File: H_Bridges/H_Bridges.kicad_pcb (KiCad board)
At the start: 2 copper layers, 59 parts, among them J1 S4B-PH-K-SLFSN, J2 USB4085-GF-A_REVB, Q1 IRF540NSTRLPBF, Q10 PMOS, Q2 IRF540NSTRLPBF, Q3 IRF540NSTRLPBF, Q4 IRF540NSTRLPBF, Q5 IRF540NSTRLPBF, Q6 IRF540NSTRLPBF, Q7 IRF540NSTRLPBF, Q8 IRF540NSTRLPBF, Q9 PMOS, U1 ESP8266, U2 max1898eub42+T, U3 TPS61023DRLR

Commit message: started placement
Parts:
- moved U1 129.9 mm to (237.8, 145.4), turned to -90 degrees
- moved R5 107.2 mm to (241.7, 74.0)
- moved R6 102.7 mm to (241.7, 67.1)
- moved R7 102.7 mm to (241.7, 69.6)
- moved R8 102.7 mm to (241.7, 72.1)
- moved FB1 97.2 mm to (64.9, 99.6)
- moved R13 89.8 mm to (55.6, 96.3), turned to 180 degrees
- moved R14 83.2 mm to (55.6, 108.1)
- moved C1 80.2 mm to (72.5, 73.6)
- moved C3 80.2 mm to (72.5, 78.6)
- moved D10 80.2 mm to (96.4, 75.2)
- moved D5 80.2 mm to (103.8, 73.3)
- moved Q10 80.2 mm to (89.2, 82.7)
- moved Q9 80.2 mm to (89.2, 78.9)
- moved R11 80.2 mm to (76.5, 81.1)
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
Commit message: finished component placement
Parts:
- removed R10, R9: 0, Resistor_SMD:R_0603_1608Metric
- moved Q7 128.0 mm to (127.0, 118.3), turned to 180 degrees
- moved D8 120.2 mm to (117.7, 113.9)
- moved R7 117.9 mm to (129.5, 105.9), turned to 90 degrees
- moved D16 109.5 mm to (106.0, 49.6), turned to 180 degrees
- moved D4 107.3 mm to (193.8, 60.1), turned to 180 degrees
- moved U1 105.3 mm to (150.0, 87.1)
- moved D15 104.8 mm to (106.0, 51.6), turned to 180 degrees
- moved Q6 103.6 mm to (144.6, 118.2), turned to 180 degrees
- moved R6 102.1 mm to (147.2, 105.8), turned to -90 degrees
- moved D14 100.1 mm to (106.0, 53.6), turned to 180 degrees
- moved D7 97.9 mm to (135.1, 113.8)
- moved Q8 95.9 mm to (179.6, 118.2), turned to 180 degrees
- moved D13 95.3 mm to (106.0, 55.7), turned to 180 degrees
- moved D1 95.3 mm to (176.3, 59.8), turned to 180 degrees
- moved Q1 91.7 mm to (166.9, 55.5)
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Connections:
- U1 pad 16: unconnected-(U1-GPIO0-Pad16) -> /P4
- U1 pad 17: unconnected-(U1-GPIO4-Pad17) -> /P3
- U1 pad 6: /P3 -> unconnected-(U1-GPIO12-Pad6)
- U1 pad 7: /P4 -> unconnected-(U1-GPIO13-Pad7)
- U1 pad 8: Net-(U1-VIN) -> unconnected-(U1-VIN-Pad8)
- U1 pad 9: Net-(U1-VBAT) -> +5V
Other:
- board outline added: 115.4 x 81.7 mm

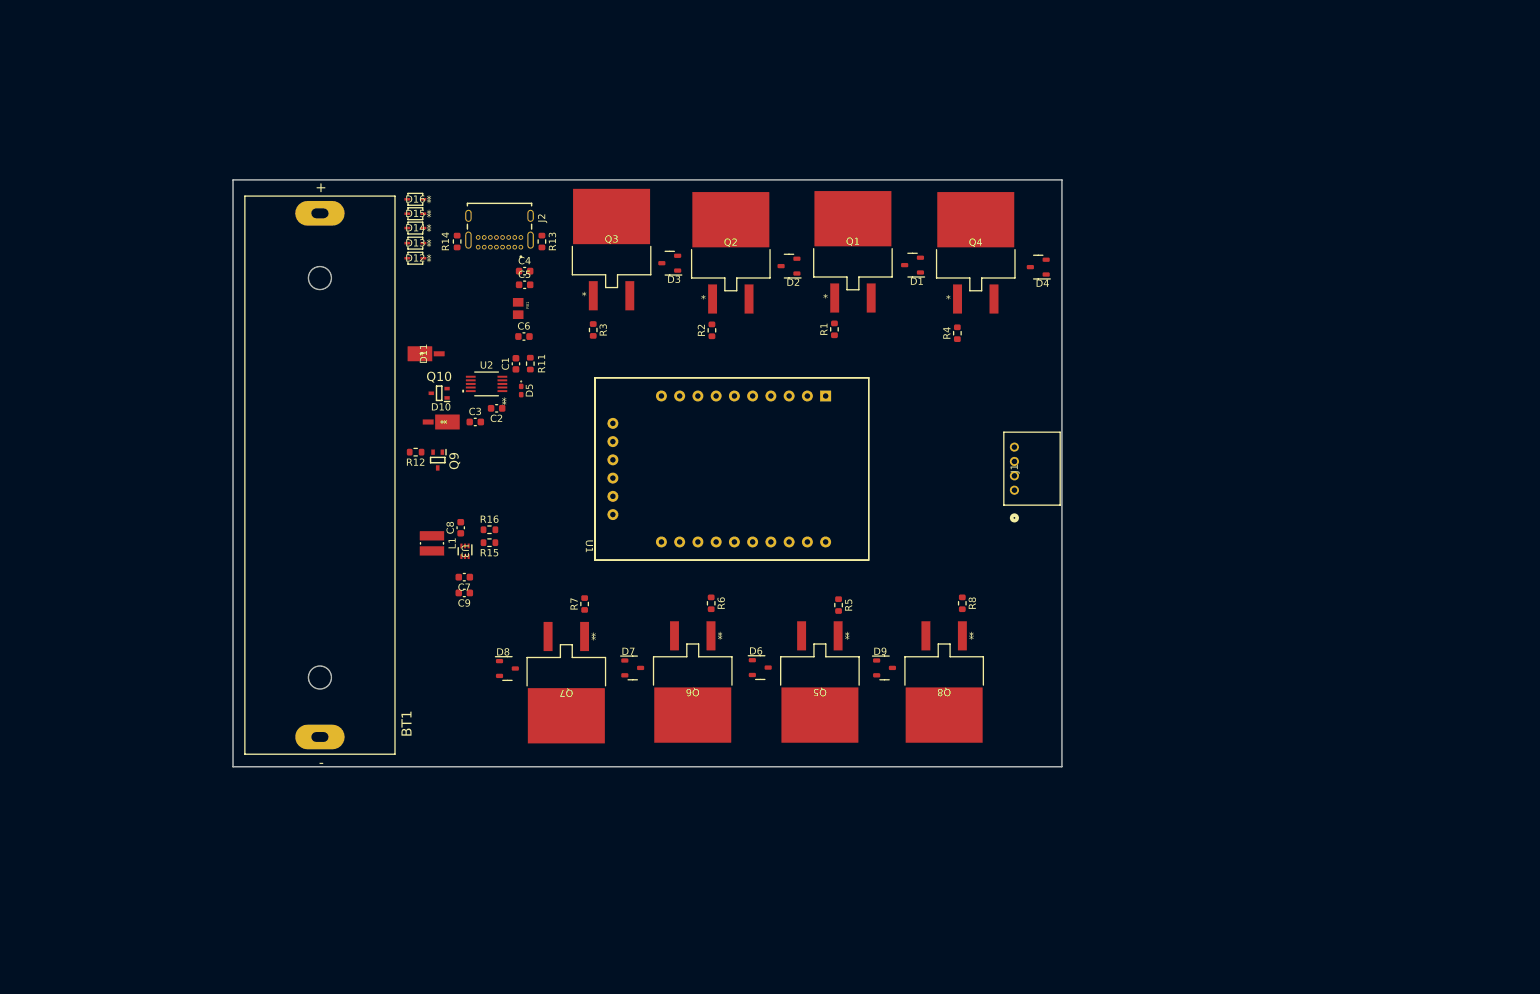
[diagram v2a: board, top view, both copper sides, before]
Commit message: placement fixes
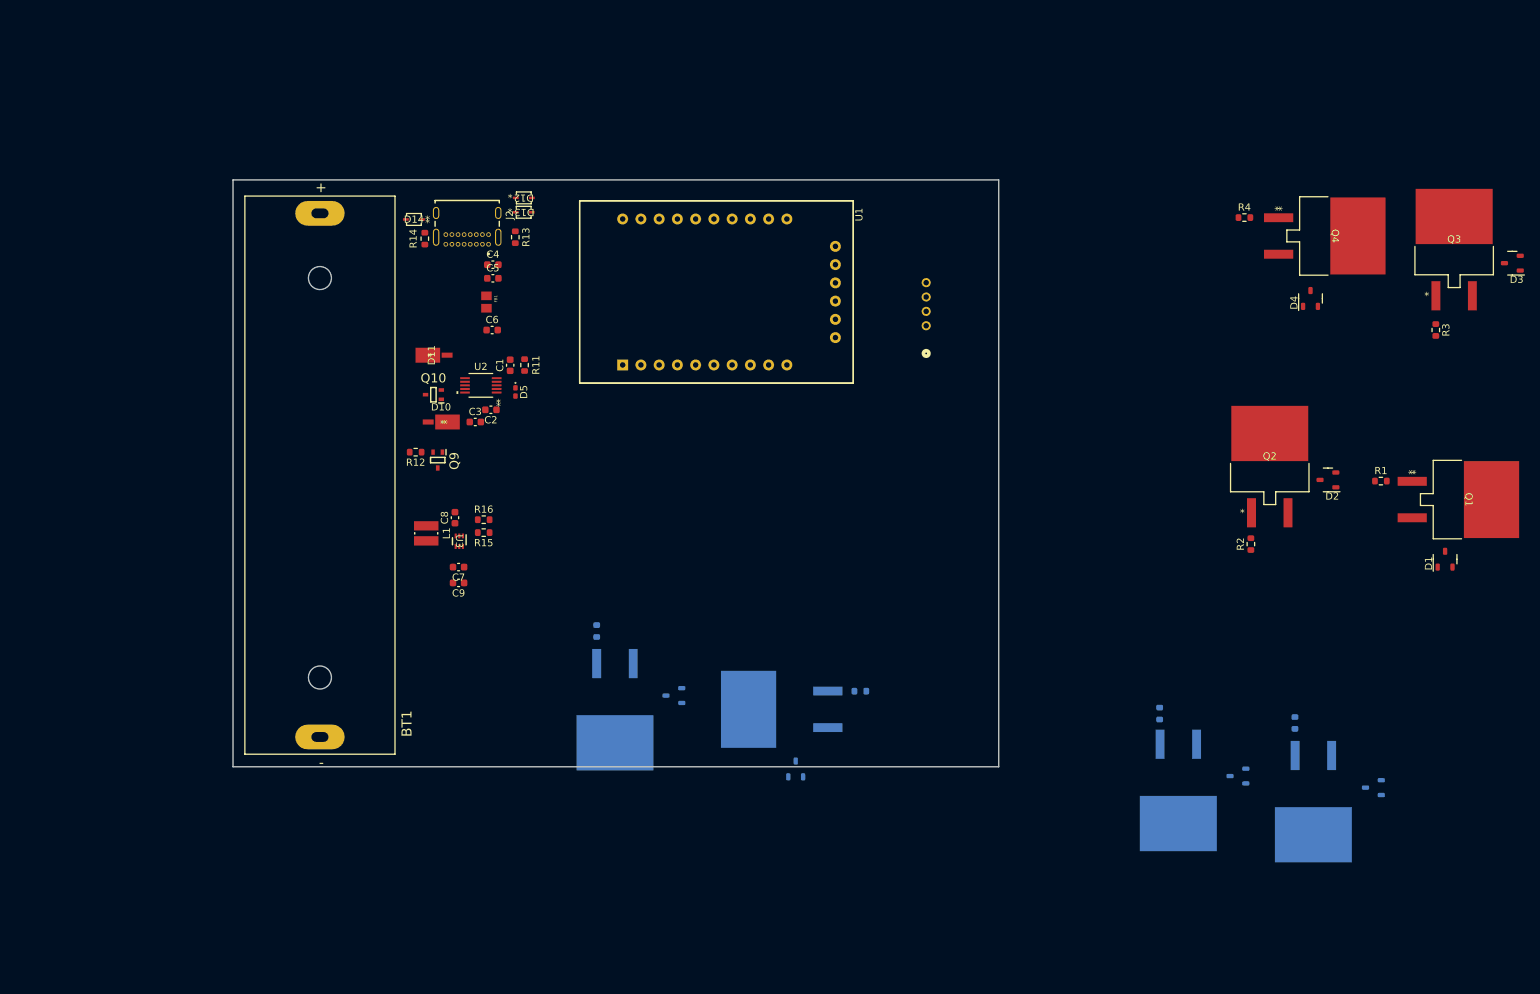
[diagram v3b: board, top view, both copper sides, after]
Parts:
- removed D15, D16: TSD05CDYFR, Footprints:TVS_SOD2_DYF_TEX-L
- D6, D7, D8, D9, J1, Q5, Q6, Q7, Q8, R5, R6, R7, R8: moved to B.Cu
- moved D3 117.3 mm to (259.8, 59.5)
- moved R3 117.3 mm to (248.0, 67.8)
- moved Q3 117.3 mm to (250.6, 55.2)
- moved D7 106.6 mm to (240.5, 130.5), turned to 180 degrees
- moved Q1 93.0 mm to (252.6, 91.4), turned to -90 degrees
- moved Q6 88.0 mm to (231.0, 134.9), turned to 0 degrees
- moved R6 83.0 mm to (228.4, 122.5)
- moved D1 82.9 mm to (248.3, 100.8), turned to 90 degrees
- moved D2 80.7 mm to (234.1, 89.7)
- moved Q2 80.7 mm to (224.9, 85.4)
- moved R2 80.7 mm to (222.3, 97.6)
- moved R1 79.0 mm to (240.4, 88.8), turned to 0 degrees
- moved D6 70.3 mm to (221.6, 128.9), turned to 180 degrees
- moved Q5 52.1 mm to (212.2, 133.3), turned to 0 degrees
- moved Q4 50.0 mm to (234.0, 54.7), turned to -90 degrees
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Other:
- board size 115.4 x 81.7 mm -> 106.6 x 81.7 mm
- copper layers 2 -> 4

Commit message: routing start
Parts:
- added G***: LOGO, LOGO, F.Cu at (183.4, 61.0)
- added H1: MountingHole, MountingHole:MountingHole_3mm_Pad_TopBottom, F.Cu at (187.3, 52.2)
- added H2: MountingHole, MountingHole:MountingHole_3mm_Pad_TopBottom, F.Cu at (85.7, 52.2)
- added H3: MountingHole, MountingHole:MountingHole_3mm_Pad_TopBottom, F.Cu at (85.7, 124.2)
- added H4: MountingHole, MountingHole:MountingHole_3mm_Pad_TopBottom, F.Cu at (187.3, 124.2)
- moved D1 116.2 mm to (132.2, 96.6), turned to -90 degrees
- moved D3 113.0 mm to (158.0, 108.6), turned to -90 degrees
- moved Q1 108.2 mm to (147.6, 117.2), turned to 180 degrees
- moved Q3 107.7 mm to (162.6, 117.2), turned to 180 degrees
- moved D2 95.4 mm to (141.0, 110.4), turned to 90 degrees
- moved R1 91.8 mm to (150.1, 105.2), turned to -90 degrees
- moved R3 90.9 mm to (165.2, 105.2), turned to 90 degrees
- moved Q2 85.3 mm to (140.1, 93.8), turned to 180 degrees
- moved R2 81.4 mm to (142.6, 81.5), turned to -90 degrees
- moved Q4 75.2 mm to (169.8, 93.8), turned to 180 degrees
- moved Q6 74.3 mm to (169.2, 93.7)
- moved R6 74.0 mm to (166.6, 81.8)
- moved D7 71.2 mm to (178.5, 95.4), turned to 90 degrees
- moved D4 60.5 mm to (178.5, 97.0), turned to -90 degrees
- moved R4 57.4 mm to (172.3, 81.9), turned to -90 degrees
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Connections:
- U1 pad 16: /P4 -> unconnected-(U1-GPIO0-Pad16)
- U1 pad 17: /P3 -> unconnected-(U1-GPIO4-Pad17)
- U1 pad 6: unconnected-(U1-GPIO12-Pad6) -> /P3
- U1 pad 7: unconnected-(U1-GPIO13-Pad7) -> /P4
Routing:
- net /Coil_B-: track 0.00 -> 28.2 mm
- net /Coil_A-: track 0.00 -> 26.5 mm
- net /Coil_A+: track 0.00 -> 25.8 mm
- net /Coil_B+: track 0.00 -> 25.8 mm
- net GND: track 0.00 -> 17.3 mm, vias 0 -> 12
- net /P4: track 0.00 -> 4.68 mm
- net /Charger/VBUS: track 0.00 -> 4.55 mm
- net +5V: vias 0 -> 16
- added copper zone on In2.Cu, net +5V
- added copper zone on In1.Cu, net GND
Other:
- board size 106.6 x 81.7 mm -> 112.4 x 81.7 mm

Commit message: power routing
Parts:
- moved G*** 88.7 mm to (120.3, 123.3), turned to 0 degrees
- moved Q7 62.3 mm to (170.8, 60.7), turned to 180 degrees
- moved Q1 59.9 mm to (169.1, 61.3), turned to 0 degrees
- moved Q5 57.7 mm to (154.1, 60.7), turned to 180 degrees
- moved Q3 56.5 mm to (154.1, 61.3), turned to 0 degrees
- moved D2 54.6 mm to (175.7, 68.1), turned to -90 degrees
- moved D1 54.3 mm to (184.5, 81.9), turned to 90 degrees
- moved D9 53.4 mm to (184.4, 83.5), turned to -90 degrees
- moved U1 52.1 mm to (160.3, 114.4), turned to -90 degrees
- moved C9 46.5 mm to (142.1, 61.6), turned to -90 degrees
- moved R8 44.4 mm to (179.2, 96.7), turned to 90 degrees
- moved R7 44.1 mm to (173.4, 73.1), turned to -90 degrees
- moved C7 43.6 mm to (139.9, 61.6), turned to -90 degrees
- moved D6 43.4 mm to (148.9, 69.7), turned to 90 degrees
- moved D4 43.1 mm to (138.2, 81.5), turned to 90 degrees
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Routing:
- net Net-(D10-K): track 0.00 -> 53.9 mm, vias 0 -> 2
- net VDD: track 0.00 -> 26.2 mm
- net VCC: track 0.00 -> 19.7 mm
- net Net-(Q10-G): track 0.00 -> 14.3 mm
- net Net-(Q10-S): track 0.00 -> 9.96 mm, vias 0 -> 2
- net /P2: track 0.00 -> 8.13 mm, vias 0 -> 1
- net GND: track 17.3 -> 24.4 mm, vias 12 -> 17
- net Net-(U2-ISET): track 0.00 -> 4.96 mm
- net Net-(D5-K): track 0.00 -> 4.34 mm
- net /P4: track 4.68 -> 0.73 mm
- net Net-(U2-CT): track 0.00 -> 2.69 mm
- net Net-(D10-A): track 0.00 -> 2.02 mm
- net /P1: track 0.00 -> 1.25 mm, vias 0 -> 1
- removed copper zone on In2.Cu, net +5V

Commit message: finished routing
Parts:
- D13, R13: moved to B.Cu
- moved D9 2.26 mm to (186.6, 84.1), turned to 90 degrees
- moved Q7 1.79 mm to (169.2, 61.3)
- moved R7 1.69 mm to (171.7, 73.2)
- moved R13 0.93 mm to (129.8, 54.8), turned to 0 degrees
- moved D13 0.50 mm to (130.1, 51.9)
- moved R2 0.39 mm to (174.1, 96.7)
- moved D14 0.32 mm to (115.1, 52.4)
- moved R5 0.09 mm to (156.7, 72.8)
- moved R3 0.06 mm to (151.6, 73.3)
- moved R14 0.06 mm to (116.2, 55.0)
- moved R6 0.05 mm to (150.1, 96.7)
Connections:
- U1 pad 4: /P1 -> /P2
- U1 pad 5: /P2 -> /P1
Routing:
- net /P3: track 0.00 -> 55.5 mm, vias 0 -> 1
- net /P1: track 1.25 -> 55.9 mm, vias 1 -> 2
- net /P4: track 0.73 -> 51.6 mm, vias 0 -> 2
- net /P2: track 8.13 -> 49.3 mm
- net GND: track 24.4 -> 42.1 mm, vias 17 -> 27
- net /Coil_B+: track 25.8 -> 37.1 mm
- net +5V: track 0.00 -> 11.2 mm, vias 16 -> 24
- net /Charger/CC1: track 0.00 -> 11.1 mm
- net /Coil_A+: track 25.8 -> 36.2 mm
- net /Coil_B-: track 28.2 -> 38.4 mm
- net /Coil_A-: track 26.5 -> 35.8 mm
- net /Charger/VBUS: track 4.55 -> 13.3 mm
- net VDD: track 26.2 -> 34.6 mm
- net /Charger/CC2: track 0.00 -> 8.14 mm
- net Net-(Q5-Pad1): track 0.00 -> 3.47 mm
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- added copper zone on In2.Cu, net +5V

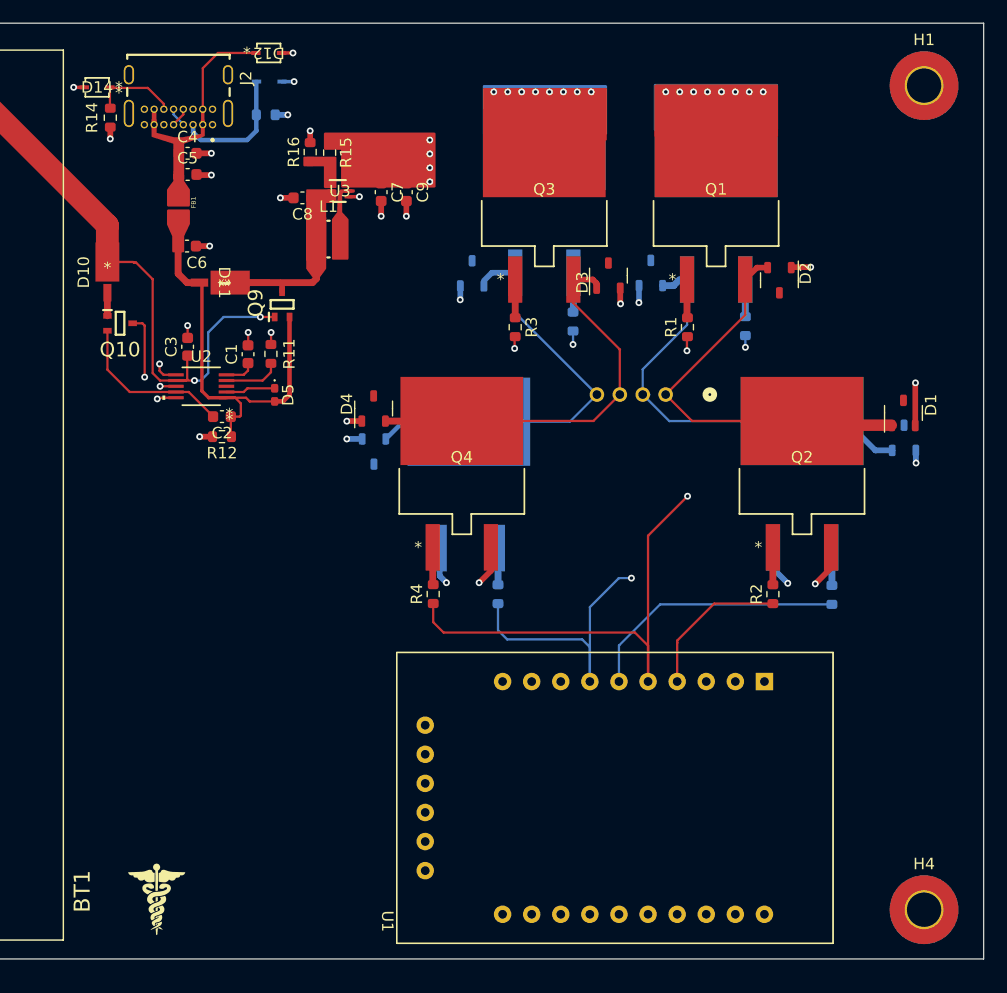
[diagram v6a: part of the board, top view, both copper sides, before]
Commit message: added sim for H-bridge
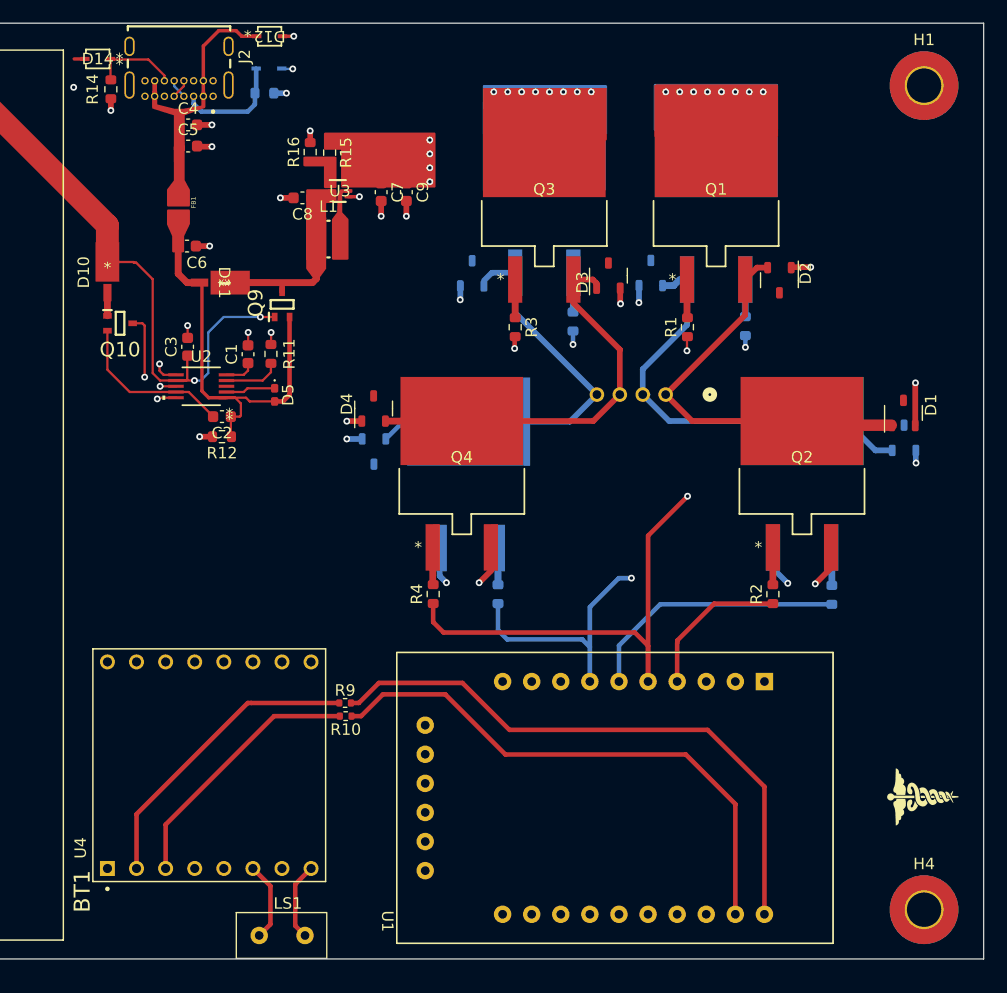
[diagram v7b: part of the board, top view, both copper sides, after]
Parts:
- added LS1: Speaker, Footprints:Speaker, F.Cu at (131.2, 126.5)
- added R10: 1k, Resistor_SMD:R_0402_1005Metric, F.Cu at (136.8, 107.3)
- added R9: 1k, Resistor_SMD:R_0402_1005Metric, F.Cu at (136.8, 106.2)
- added U4: ~, Footprints:MODULE_DFR0299, F.Cu at (124.9, 111.6)
- moved G*** 67.5 mm to (187.2, 114.3), turned to 90 degrees
- moved D14 2.48 mm to (115.2, 49.9)
- moved C4 2.48 mm to (123.0, 55.7)
- moved C5 2.48 mm to (123.0, 57.5)
- moved J2 2.48 mm to (122.2, 48.8)
- moved R14 2.48 mm to (116.3, 52.6)
- moved R13 1.89 mm to (129.7, 52.9)
- moved D12 1.46 mm to (130.2, 47.9)
- moved D13 1.14 mm to (130.1, 50.8)
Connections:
- U1 pad 19: unconnected-(U1-RXD-Pad19) -> /MP3_TX
- U1 pad 20: unconnected-(U1-TXD-Pad20) -> /MP3_RX
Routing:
- net /MP3_RX: track 0.00 -> 51.7 mm
- net /MP3_TX: track 0.00 -> 47.9 mm
- net Net-(U4-RX): track 0.00 -> 26.5 mm
- net Net-(U4-TX): track 0.00 -> 23.0 mm
- net /SPK+: track 0.00 -> 6.89 mm
- net /SPK-: track 0.00 -> 6.77 mm
- net /Charger/CC1: track 11.1 -> 9.73 mm
- added copper zone on In2.Cu, net +3V3
